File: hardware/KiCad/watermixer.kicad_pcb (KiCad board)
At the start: 2 copper layers, 147.3 x 100 mm, 21 parts, among them U1 CR2013-MI2120-touch, U2 ESP32-DevKitC, U3 LLC_4CH, U4 MCP4728

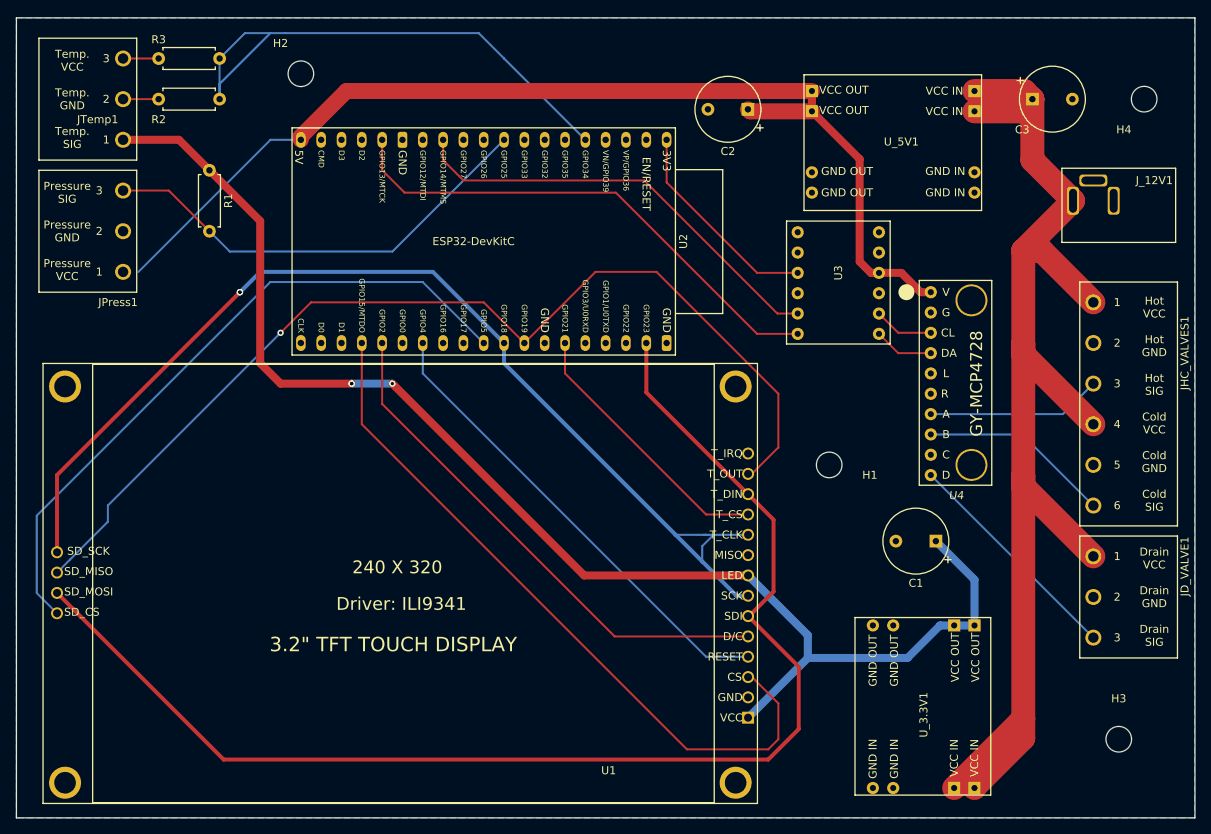
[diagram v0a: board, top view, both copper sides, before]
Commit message: starting to add an ADC
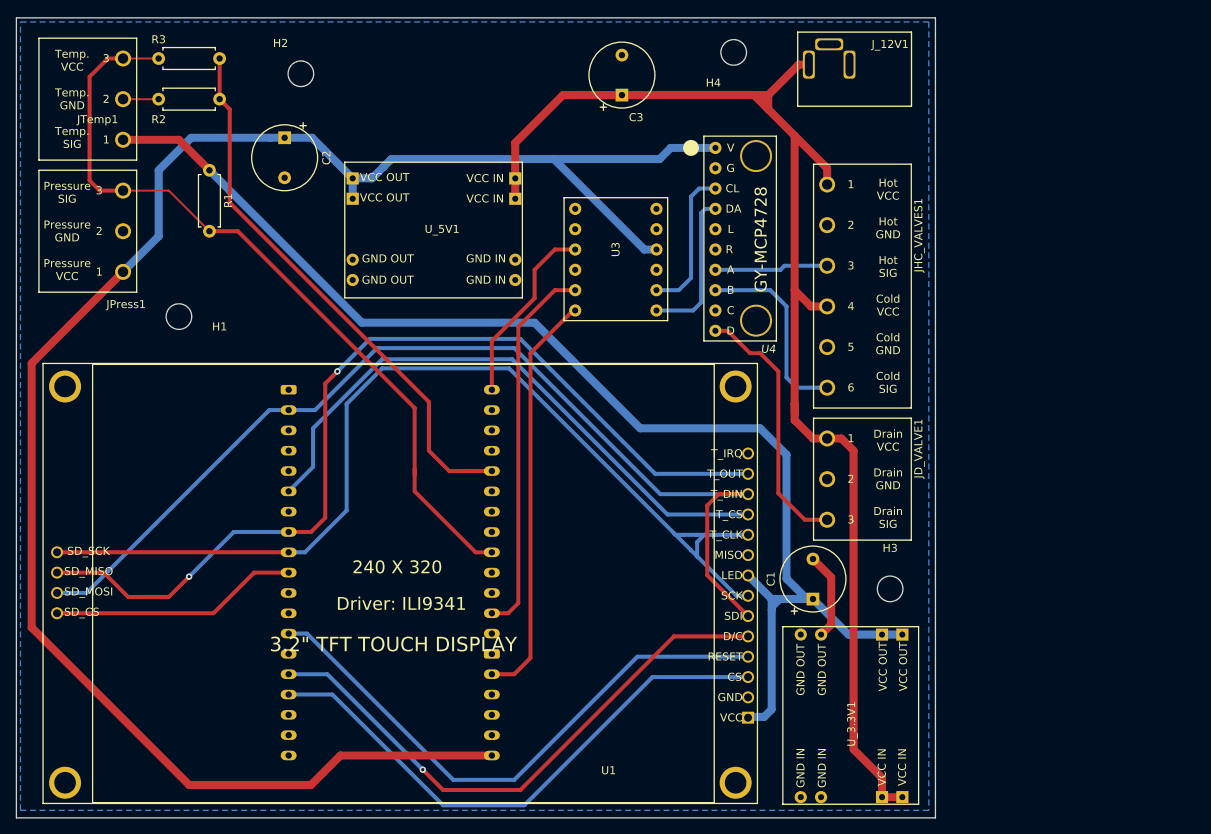
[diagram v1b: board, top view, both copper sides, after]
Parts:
- U2: moved to B.Cu
- moved H1 83.4 mm to (91.4, 62.7)
- moved U_5V1 58.4 mm to (134.4, 60.5)
- moved C2 58.0 mm to (104.6, 40.4), turned to 270 degrees
- moved H4 51.6 mm to (160.8, 29.7)
- moved C3 51.3 mm to (146.8, 35.1), turned to 90 degrees
- moved U2 38.1 mm to (130.6, 71.9), turned to 180 degrees
- moved J_12V1 37.1 mm to (182.9, 36.3)
- moved JD_VALVE1 36.4 mm to (172.5, 75.4)
- moved JHC_VALVES1 36.4 mm to (172.5, 43.7)
- moved H3 34.2 mm to (180.3, 96.8)
- moved U4 32.4 mm to (166.1, 67.1)
- moved U3 28.0 mm to (152.5, 47.9)
- moved C1 17.0 mm to (170.7, 98.0), turned to 90 degrees
- moved U_3.3V1 9.09 mm to (166.9, 123.7)
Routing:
- net VDDF: track 136.2 -> 225.9 mm
- net Net-(U1-Pad10): track 84.4 -> 31.1 mm
- net Net-(U1-Pad15): track 34.0 -> 75.1 mm
- net /SIG: track 61.0 -> 98.9 mm
- net Net-(U1-Pad11): track 161.5 -> 128.2 mm
- net Net-(U1-Pad3): track 88.7 -> 69.8 mm
- net Net-(U1-Pad4): track 59.1 -> 76.6 mm
- net Net-(U2-Pad15): track 64.2 -> 51.1 mm
- net Net-(U3-Pad11): track 7.48 -> 19.2 mm
- net Net-(U1-Pad12): track 129.0 -> 117.8 mm, vias 1 -> 3
- net Net-(U3-Pad9): track 7.48 -> 18.6 mm
- net GND: track 4.45 -> 15.4 mm
- net Net-(U1-Pad13): track 138.1 -> 127.8 mm, vias 2 -> 0
- net VDD: track 170.1 -> 160.4 mm, vias 3 -> 0
- net Net-(JHC_VALVES1-Pad3): track 21.9 -> 14.2 mm
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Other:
- board size 147.3 x 100 mm -> 114.9 x 100 mm

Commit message: added ADS1115 to pcb and ordered 5 pcbs with current production
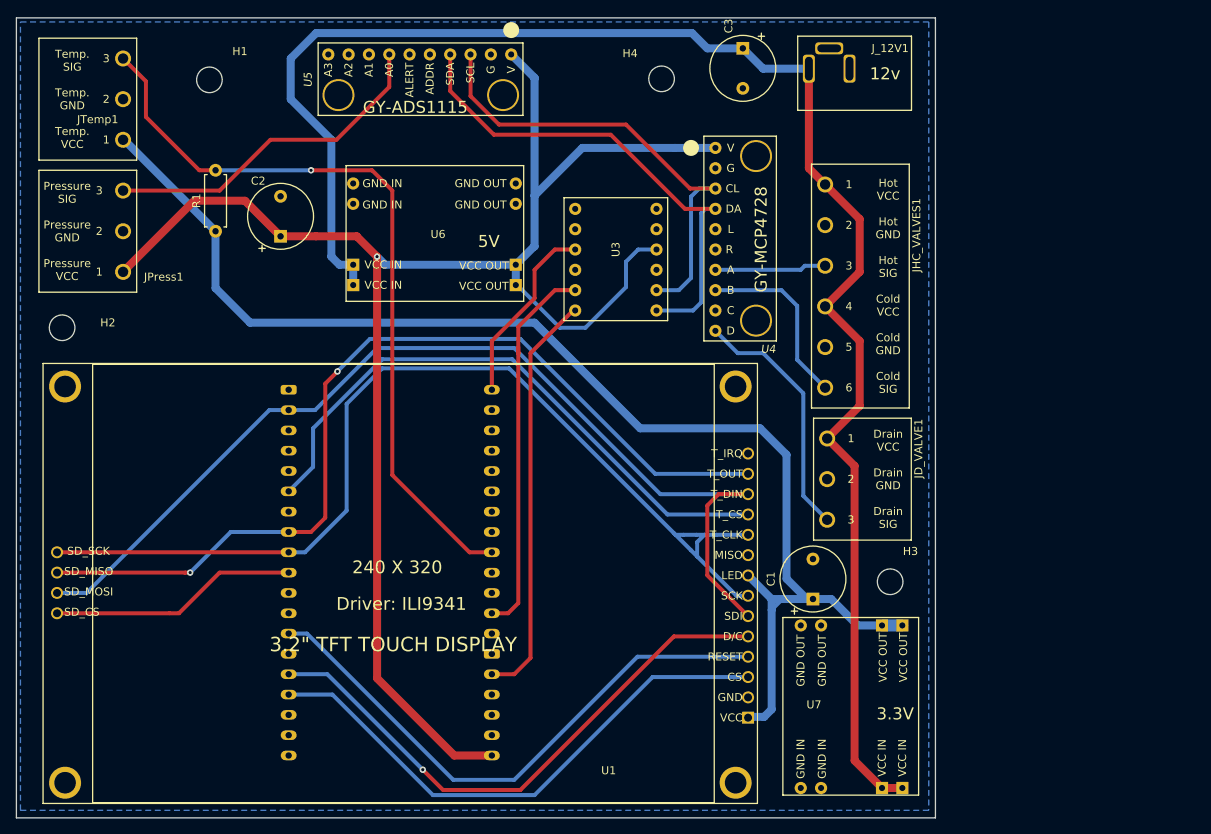
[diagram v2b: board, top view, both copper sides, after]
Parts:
- removed R2: 4.7k, Resistor_THT:R_Axial_DIN0207_L6.3mm_D2.5mm_P7.62mm_Horizontal
- removed R3: 3.3k, Resistor_THT:R_Axial_DIN0207_L6.3mm_D2.5mm_P7.62mm_Horizontal
- removed U_3.3V1, U_5V1: SD_BUCK3A, watermixer-footprints:SD_BUCK3A
- added U5: ADS1115, watermixer-footprints:ADS1115_module, F.Cu at (107.6, 37.6)
- added U6: SD_BUCK3A, watermixer-footprints:SD_BUCK3A, F.Cu at (112.3, 43.8)
- added U7: SD_BUCK3A, watermixer-footprints:SD_BUCK3A, F.Cu at (166.9, 122.6)
- moved H2 43.6 mm to (76.8, 64.1)
- moved H1 29.8 mm to (95.2, 33.1)
- moved C3 16.2 mm to (161.9, 29.2), turned to 270 degrees
- moved C2 12.3 mm to (104.1, 52.7), turned to 90 degrees
- moved H4 9.60 mm to (151.8, 33.0)
- moved R1 7.66 mm to (96.0, 52.1), turned to 90 degrees
- moved H3 0.89 mm to (180.3, 95.9)
- moved J_12V1 0.51 mm to (182.9, 36.8)
- moved JHC_VALVES1 0.25 mm to (172.2, 43.7)
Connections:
- net VCC renamed +12V
- net VDD renamed +3V3
- net VDDF renamed +5V
- JPress1 pad 3: /SIG -> /SIGP
- JTemp1 pad 3: /SIG -> /SIGT
- R1 pad 2: /SIG -> /SIGT
- U1 pad 18: Net-(U1-Pad18) -> (no net)
- U1 pad 9: Net-(U1-Pad9) -> (no net)
- U2 pad 10: Net-(U2-Pad10) -> (no net)
- U2 pad 11: Net-(U2-Pad11) -> (no net)
- U2 pad 13: Net-(U2-Pad13) -> (no net)
- U2 pad 16: Net-(U2-Pad16) -> (no net)
- U2 pad 17: Net-(U2-Pad17) -> (no net)
- U2 pad 18: Net-(U2-Pad18) -> (no net)
- U2 pad 2: Net-(U2-Pad2) -> (no net)
- U2 pad 20: Net-(U2-Pad20) -> (no net)
- U2 pad 21: Net-(U2-Pad21) -> (no net)
- U2 pad 22: Net-(U2-Pad22) -> (no net)
- U2 pad 25: Net-(U2-Pad25) -> (no net)
- U2 pad 27: Net-(U2-Pad27) -> (no net)
- U2 pad 28: Net-(U2-Pad28) -> (no net)
- U2 pad 3: Net-(U2-Pad3) -> (no net)
- U2 pad 34: Net-(U2-Pad34) -> (no net)
- U2 pad 35: Net-(U2-Pad35) -> (no net)
- U2 pad 36: Net-(U2-Pad36) -> (no net)
- U2 pad 4: Net-(U2-Pad4) -> (no net)
- U2 pad 5: Net-(R2-Pad2) -> (no net)
- U2 pad 6: Net-(U2-Pad6) -> (no net)
- U2 pad 7: Net-(U2-Pad7) -> (no net)
- U2 pad 8: Net-(U2-Pad8) -> (no net)
- U2 pad 9: /SIG -> /SIGT
- U3 pad 4: Net-(U3-Pad4) -> (no net)
- U3 pad 5: Net-(U3-Pad5) -> (no net)
- U3 pad 6: Net-(U3-Pad6) -> (no net)
- U3 pad 7: Net-(U3-Pad7) -> (no net)
- U4 pad 4: Net-(U4-Pad4) -> (no net)
- U4 pad 5: Net-(U4-Pad5) -> (no net)
- U4 pad 8: Net-(U4-Pad8) -> (no net)
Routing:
- net /SIG: track 98.9 -> 0.00 mm
- net /SIGT: track 0.00 -> 95.1 mm, vias 0 -> 1
- net Net-(R2-Pad2): track 68.8 -> 0.00 mm
- net Net-(U3-Pad11): track 19.2 -> 63.0 mm
- net /SIGP: track 0.00 -> 42.7 mm
- net +12V: track 162.5 -> 203.7 mm
- net Net-(U3-Pad9): track 18.6 -> 59.2 mm
- net +5V: track 225.9 -> 209.1 mm, vias 0 -> 1
- net GND: track 15.4 -> 0.00 mm
- net +3V3: track 160.4 -> 164.1 mm
- net Net-(U1-Pad12): track 117.8 -> 115.3 mm
- net Net-(JHC_VALVES1-Pad6): track 24.2 -> 22.7 mm
- net Net-(JD_VALVE1-Pad3): track 32.7 -> 31.3 mm
- net Net-(U1-Pad3): track 69.8 -> 68.7 mm
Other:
- board text added: "12v"
- board text added: "3.3V"
- board text added: "5V"
- board text added: "Temp. SIG Temp. GND Temp. VCC"
- board text removed: "Temp. VCC Temp. GND Temp. SIG"
